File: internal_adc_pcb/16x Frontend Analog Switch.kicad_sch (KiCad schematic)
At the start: 26 parts, among them U1 RS2323XUTQK10, U2 RS2323XUTQK10, U3 RS2323XUTQK10, U4 RS2323XUTQK10, U5 RS2323XUTQK10, U6 RS2323XUTQK10, U7 RS2323XUTQK10, U8 RS2323XUTQK10

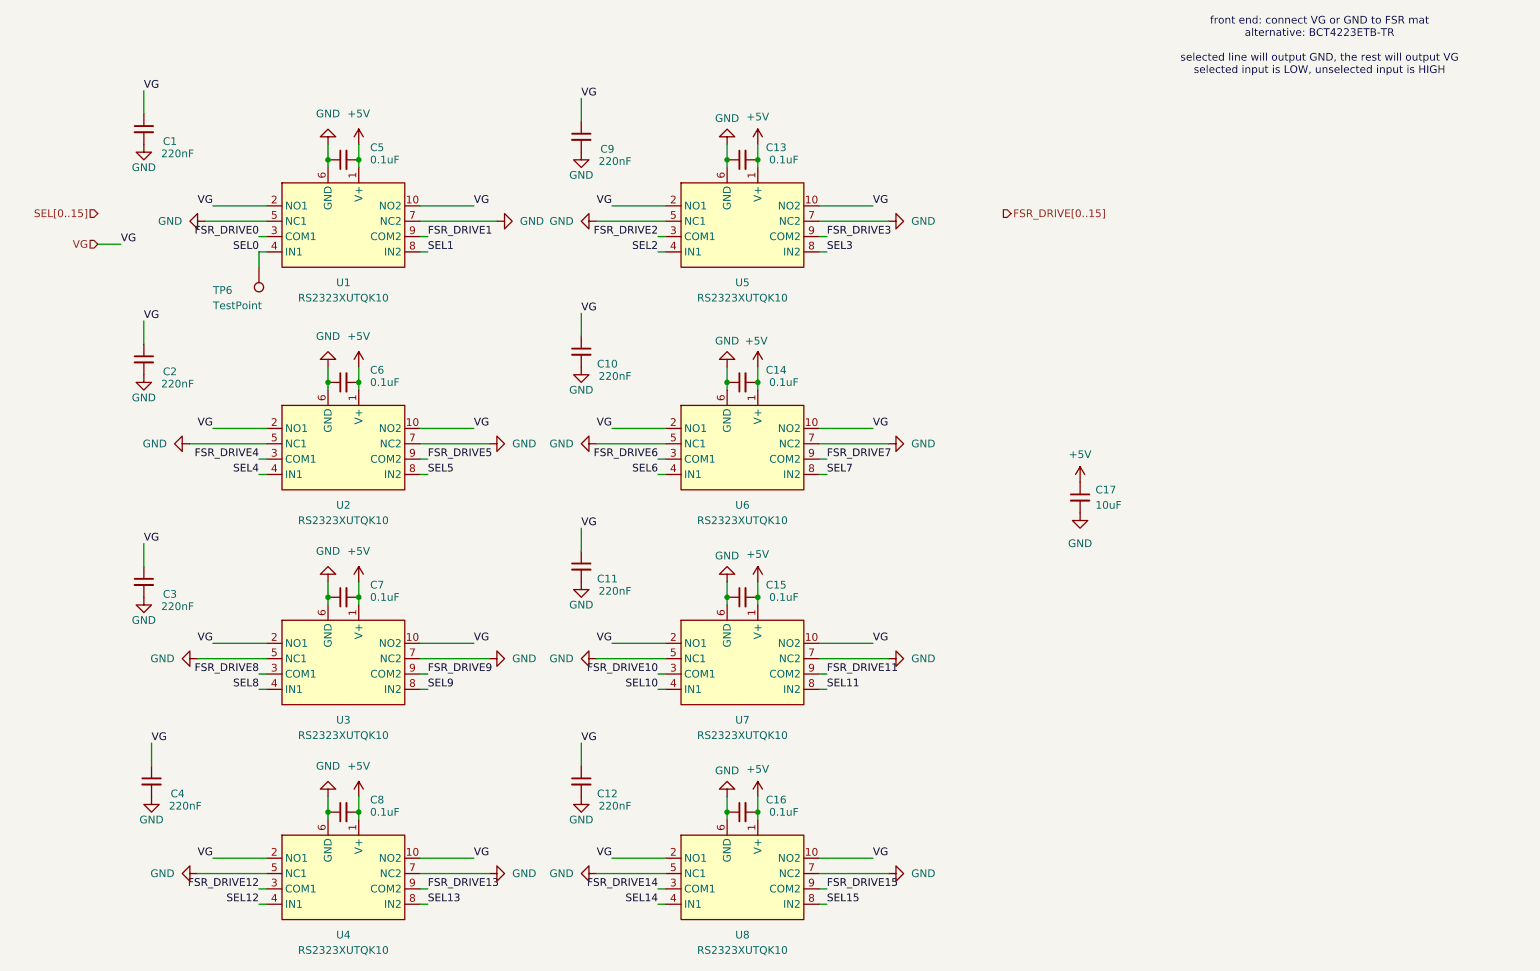
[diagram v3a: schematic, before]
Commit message: fixing all ERC errors for internal ADC ver, fixing warnings now
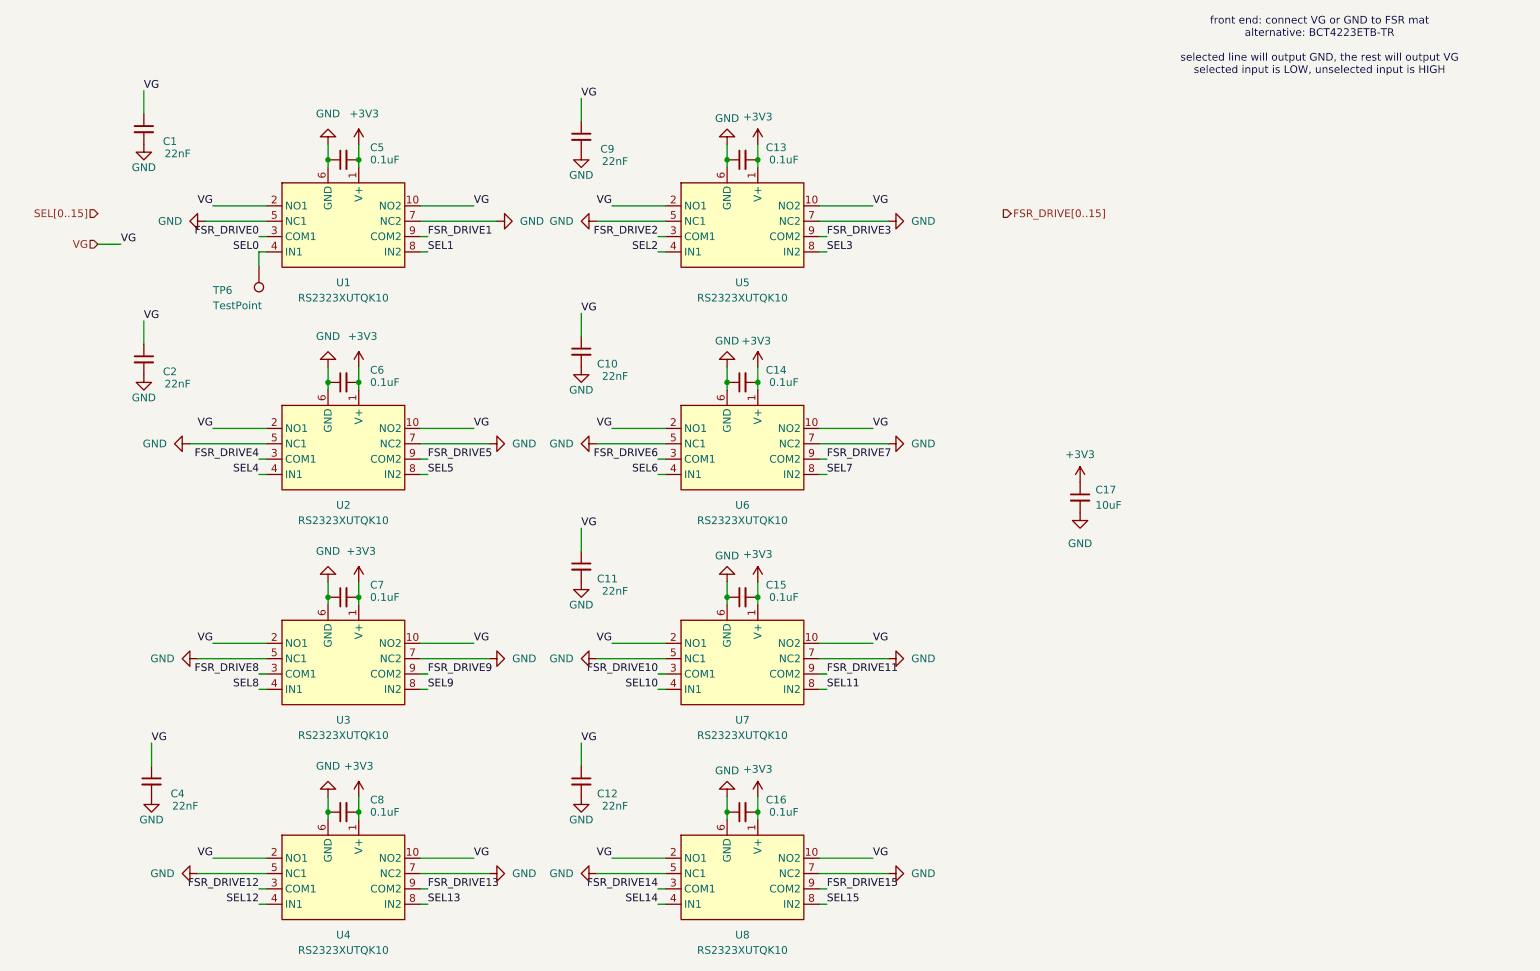
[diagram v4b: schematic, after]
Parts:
- removed C3: 220nF, Capacitor_SMD:C_0603_1608Metric, symbol Device:C_Small
- C1, C10, C11, C12, C2, C4, C9: value 220nF -> 22nF
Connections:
- net +5V renamed +3V3
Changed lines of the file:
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@@
 	(wire
 		(pts
-			(xy 44.45 109.22) (xy 44.45 105.41)
-		)
-		(stroke
-			(width 0)
-			(type default)
-		)
-	)
-	(wire
-		(pts
 			(xy 63.5 165.1) (xy 64.77 165.1)
 		)
@@
 	)
 	(label "VG"
-		(at 44.45 105.41 0)
-		(effects
-			(font
-				(face "Iosevka NF")
-				(size 1.27 1.27)
-			)
-			(justify left bottom)
-		)
-	)
-	(label "VG"
 		(at 55.88 49.53 180)
 		(effects
@@
 		(in_pos_files yes)
 		(dnp no)
-		(fields_autoplaced yes)
 		(property "Reference" "#PWR015"
 			(at 80.01 115.57 0)
@@
 			)
 		)
-		(property "Value" "+5V"
-			(at 80.01 106.68 0)
+		(property "Value" "+3V3"
+			(at 77.978 106.68 0)
 			(show_name no)
 			(do_not_autoplace no)
@@
 					(size 1.27 1.27)
 				)
+				(justify left)
 			)
 		)
@@
 			)
 		)
-		(property "Value" "220nF"
+		(property "Value" "22nF"
 			(at 122.428 148.844 0)
 			(show_name no)
@@
 	(symbol
 		(lib_id "power:GND")
-		(at 44.45 114.3 0)
-		(unit 1)
-		(body_style 1)
-		(exclude_from_sim no)
-		(in_bom yes)
-		(on_board yes)
-		(in_pos_files yes)
-		(dnp no)
-		(property "Reference" "#PWR03"
-			(at 44.45 120.65 0)
-			(hide yes)
-			(show_name no)
-			(do_not_autoplace no)
-			(effects
-				(font
-					(face "Iosevka NF")
-					(size 1.27 1.27)
-				)
-			)
-		)
-		(property "Value" "GND"
-			(at 44.45 118.11 0)
-			(show_name no)
-			(do_not_autoplace no)
-			(effects
-				(font
-					(face "Iosevka NF")
-					(size 1.27 1.27)
-				)
-			)
-		)
-		(property "Footprint" ""
-			(at 44.45 114.3 0)
-			(hide yes)
-			(show_name no)
-			(do_not_autoplace no)
-			(effects
-				(font
-					(face "Iosevka NF")
-					(size 1.27 1.27)
-				)
-			)
-		)
-		(property "Datasheet" ""
-			(at 44.45 114.3 0)
-			(hide yes)
-			(show_name no)
-			(do_not_autoplace no)
-			(effects
-				(font
-					(face "Iosevka NF")
-					(size 1.27 1.27)
-				)
-			)
-		)
-		(property "Description" "Power symbol creates a global label with name \"GND\" , ground"
-			(at 44.45 114.3 0)
-			(hide yes)
-			(show_name no)
-			(do_not_autoplace no)
-			(effects
-				(font
-					(face "Iosevka NF")
-					(size 1.27 1.27)
-				)
-			)
-		)
-		(pin "1"
-		)
-		(instances
-			(project "FSR_matrix_readout"
-				(path "/6dca5e5c-f676-465d-98c9-14af6047a226/0257cdfa-5088-43ef-b3f9-44ecadae8ca2"
-					(reference "#PWR018")
-					(unit 1)
-				)
-			)
-			(project "fsr_matrix_readout_internal_adc"
-				(path "/a2a8c34e-3adf-4a95-8857-b713f7048029/307fdc1f-8268-4192-8310-111e61425162"
-					(reference "#PWR03")
-					(unit 1)
-				)
-			)
-		)
-	)
-	(symbol
-		(lib_id "power:GND")
 		(at 167.64 88.9 90)
 		(unit 1)
@@
 			)
 		)
-		(property "Value" "220nF"
+		(property "Value" "22nF"
 			(at 122.428 77.724 0)
 			(show_name no)
@@
 			)
 		)
-		(property "Value" "+5V"
+		(property "Value" "+3V3"
 			(at 146.05 34.798 0)
 			(show_name no)
@@
 			)
 		)
-		(property "Value" "220nF"
+		(property "Value" "22nF"
 			(at 122.428 113.284 0)
 			(show_name no)
@@
 			)
 		)
-		(property "Value" "+5V"
+		(property "Value" "+3V3"
 			(at 146.05 107.188 0)
 			(show_name no)
@@
 			)
 		)
-		(property "Value" "220nF"
+		(property "Value" "22nF"
 			(at 50.038 78.994 0)
 			(show_name no)
@@
 			)
 		)
-		(property "Value" "+5V"
+		(property "Value" "+3V3"
 			(at 145.796 71.882 0)
 			(show_name no)
@@
 			)
 		)
-		(property "Value" "+5V"
+		(property "Value" "+3V3"
 			(at 199.39 90.678 0)
 			(show_name no)
@@
 	)
 	(symbol
-		(lib_id "Device:C_Small")
-		(at 44.45 111.76 0)
-		(unit 1)
-		(body_style 1)
-		(exclude_from_sim no)
-		(in_bom yes)
-		(on_board yes)
-		(in_pos_files yes)
-		(dnp no)
-		(property "Reference" "C3"
-			(at 48.768 113.792 0)
-			(show_name no)
-			(do_not_autoplace no)
-			(effects
-				(font
-					(face "Iosevka NF")
-					(size 1.27 1.27)
-				)
-			)
-		)
-		(property "Value" "220nF"
-			(at 50.038 115.824 0)
-			(show_name no)
-			(do_not_autoplace no)
-			(effects
-				(font
-					(face "Iosevka NF")
-					(size 1.27 1.27)
-				)
-			)
-		)
-		(property "Footprint" "Capacitor_SMD:C_0603_1608Metric"
-			(at 44.45 111.76 0)
-			(hide yes)
-			(show_name no)
-			(do_not_autoplace no)
-			(effects
-				(font
-					(face "Iosevka NF")
-					(size 1.27 1.27)
-				)
-			)
-		)
-		(property "Datasheet" ""
-			(at 44.45 111.76 0)
-			(hide yes)
-			(show_name no)
-			(do_not_autoplace no)
-			(effects
-				(font
-					(face "Iosevka NF")
-					(size 1.27 1.27)
-				)
-			)
-		)
-		(property "Description" "Unpolarized capacitor, small symbol"
-			(at 44.45 111.76 0)
-			(hide yes)
-			(show_name no)
-			(do_not_autoplace no)
-			(effects
-				(font
-					(face "Iosevka NF")
-					(size 1.27 1.27)
-				)
-			)
-		)
-		(pin "1"
-		)
-		(pin "2"
-		)
-		(instances
-			(project "FSR_matrix_readout"
-				(path "/6dca5e5c-f676-465d-98c9-14af6047a226/0257cdfa-5088-43ef-b3f9-44ecadae8ca2"
-					(reference "C9")
-					(unit 1)
-				)
-			)
-			(project "fsr_matrix_readout_internal_adc"
-				(path "/a2a8c34e-3adf-4a95-8857-b713f7048029/307fdc1f-8268-4192-8310-111e61425162"
-					(reference "C3")
-					(unit 1)
-				)
-			)
-		)
-	)
-	(symbol
 		(lib_id "lcsc:RS2323XUTQK10")
 		(at 77.47 125.73 0)
@@
 		(in_pos_files yes)
 		(dnp no)
-		(fields_autoplaced yes)
 		(property "Reference" "#PWR014"
 			(at 80.01 80.01 0)
@@
 			)
 		)
-		(property "Value" "+5V"
-			(at 80.01 71.12 0)
+		(property "Value" "+3V3"
+			(at 78.232 71.12 0)
 			(show_name no)
 			(do_not_autoplace no)
@@
 					(size 1.27 1.27)
 				)
+				(justify left)
 			)
 		)
@@
 			)
 		)
-		(property "Value" "+5V"
+		(property "Value" "+3V3"
 			(at 146.05 142.748 0)
 			(show_name no)
@@
 			)
 		)
-		(property "Value" "220nF"
+		(property "Value" "22nF"
 			(at 50.038 40.894 0)
 			(show_name no)
@@
 			)
 		)
-		(property "Value" "220nF"
+		(property "Value" "22nF"
 			(at 122.428 42.164 0)
 			(show_name no)
@@
 			)
 		)
-		(property "Value" "220nF"
+		(property "Value" "22nF"
 			(at 51.308 148.844 0)
 			(show_name no)
@@
 		(in_pos_files yes)
 		(dnp no)
-		(fields_autoplaced yes)
 		(property "Reference" "#PWR013"
 			(at 80.01 43.18 0)
@@
 			)
 		)
-		(property "Value" "+5V"
-			(at 80.01 34.29 0)
+		(property "Value" "+3V3"
+			(at 78.486 34.29 0)
 			(show_name no)
 			(do_not_autoplace no)
@@
 					(size 1.27 1.27)
 				)
+				(justify left)
 			)
 		)
@@
 			)
 		)
-		(property "Value" "+5V"
+		(property "Value" "+3V3"
 			(at 80.01 142.24 0)
 			(show_name no)
